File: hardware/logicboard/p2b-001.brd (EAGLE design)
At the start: 91 x 90 mm, 54 parts, among them IC1 74LS06N, IC2 4066N, J1 MKR, J2 GPIO, J3 Vcc, J4 RLY, J5 SPI, J7 DIN5, J8 DIN5, J9 DIN5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

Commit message: Renumbered signal names and silk patterns.
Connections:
- removed net ANLG4: IC2.11, MC1.P$28, RN1.5
- removed net DTCT4: MC1.P$1, SV1.15, SV3.14
- removed net GPIO2: J2.3, MC1.P$5, SV3.10
- removed net LED2: MC1.P$2, R5.2, SV2.17
- new net ANLG0: IC2.1, MC1.P$31, RN1.2
- new net DTCT0: MC1.P$7, SV1.3, SV3.11
- new net GPIO0: J2.2, MC1.P$8, SV3.9
- new net LED0: MC1.P$34, R4.2, SV2.9
- net ANLG1: now also IC2.4, MC1.P$30, RN1.3; no longer IC2.1, MC1.P$31, RN1.2
- net ANLG2: now also IC2.8, MC1.P$29, RN1.4; no longer IC2.4, MC1.P$30, RN1.3
- net ANLG3: now also IC2.11, MC1.P$28, RN1.5; no longer IC2.8, MC1.P$29, RN1.4
- net DTCT1: now also MC1.P$4, SV1.7, SV3.12; no longer MC1.P$7, SV1.3, SV3.11
- net DTCT2: now also MC1.P$3, SV1.11, SV3.13; no longer MC1.P$4, SV1.7, SV3.12
- net DTCT3: now also MC1.P$1, SV1.15, SV3.14; no longer MC1.P$3, SV1.11, SV3.13
- net GPIO1: now also J2.3, MC1.P$5, SV3.10; no longer J2.2, MC1.P$8, SV3.9
- net LED1: now also MC1.P$2, R5.2, SV2.17; no longer MC1.P$34, R4.2, SV2.9
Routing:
- net GPIO2: track 146.6 -> 0.00 mm, vias 2 -> 0
- net LED0: track 0.00 -> 141.5 mm, vias 0 -> 4
- net GPIO0: track 0.00 -> 118.0 mm, vias 0 -> 2
- net LED2: track 115.8 -> 0.00 mm
- net DTCT4: track 99.1 -> 0.00 mm, vias 2 -> 0
- net ANLG4: track 97.6 -> 0.00 mm, vias 4 -> 0
- net DTCT0: track 0.00 -> 77.0 mm, vias 0 -> 4
- net ANLG0: track 0.00 -> 64.4 mm, vias 0 -> 5
- net ANLG1: track 64.4 -> 96.4 mm, vias 5 -> 3
- net GPIO1: track 118.0 -> 146.6 mm
- net DTCT2: track 85.3 -> 112.2 mm, vias 3 -> 4
- net LED1: track 141.5 -> 115.8 mm, vias 4 -> 0
- net DTCT3: track 112.2 -> 99.1 mm, vias 4 -> 2
- net DTCT1: track 77.0 -> 85.3 mm, vias 4 -> 3
- net ANLG2: track 96.4 -> 103.3 mm, vias 3 -> 7
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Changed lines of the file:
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@@
 <grid distance="0.5" unitdist="mm" unit="mm" style="lines" multiple="2" display="yes" altdistance="50" altunitdist="mil" altunit="mil"/>
 <layers>
-<layer number="1" name="Top" color="4" fill="1" visible="yes" active="yes"/>
-<layer number="16" name="Bottom" color="1" fill="1" visible="yes" active="yes"/>
+<layer number="1" name="Top" color="4" fill="1" visible="no" active="yes"/>
+<layer number="16" name="Bottom" color="1" fill="1" visible="no" active="yes"/>
 <layer number="17" name="Pads" color="2" fill="1" visible="yes" active="yes"/>
 <layer number="18" name="Vias" color="2" fill="1" visible="yes" active="yes"/>
@@
 <wire x1="12.954" y1="31.5468" x2="13" y2="31.5" width="0.1524" layer="16"/>
 </signal>
-<signal name="ANLG4" class="3">
+<signal name="ANLG3" class="3">
 <contactref element="MC1" pad="P$28"/>
 <contactref element="IC2" pad="11"/>
@@
 <via x="59.5122" y="46.482" extent="1-16" drill="0.3048"/>
 </signal>
-<signal name="ANLG3" class="3">
+<signal name="ANLG2" class="3">
 <contactref element="MC1" pad="P$29"/>
 <contactref element="IC2" pad="8"/>
@@
 <via x="35.5092" y="77.1906" extent="1-16" drill="0.3048"/>
 </signal>
-<signal name="ANLG2" class="3">
+<signal name="ANLG1" class="3">
 <contactref element="MC1" pad="P$30"/>
 <contactref element="IC2" pad="4"/>
@@
 <via x="58.5216" y="82.9818" extent="1-16" drill="0.3048"/>
 </signal>
-<signal name="ANLG1" class="3">
+<signal name="ANLG0" class="3">
 <contactref element="MC1" pad="P$31"/>
 <contactref element="IC2" pad="1"/>
@@
 <wire x1="44.577" y1="65.4558" x2="44.62" y2="65.5" width="0.1524" layer="16"/>
 </signal>
-<signal name="DTCT1">
+<signal name="DTCT0">
 <contactref element="MC1" pad="P$7"/>
 <contactref element="SV1" pad="3"/>
@@
 <via x="50.0634" y="61.2648" extent="1-16" drill="0.3048"/>
 </signal>
-<signal name="DTCT2">
+<signal name="DTCT1">
 <contactref element="MC1" pad="P$4"/>
 <contactref element="SV1" pad="7"/>
@@
 <via x="49.2252" y="76.7334" extent="1-16" drill="0.3048"/>
 </signal>
-<signal name="DTCT3">
+<signal name="DTCT2">
 <contactref element="MC1" pad="P$3"/>
 <contactref element="SV1" pad="11"/>
@@
 <via x="39.0144" y="62.484" extent="1-16" drill="0.3048"/>
 </signal>
-<signal name="DTCT4">
+<signal name="DTCT3">
 <contactref element="MC1" pad="P$1"/>
 <contactref element="SV1" pad="15"/>
@@
 <via x="69.342" y="27.8892" extent="1-16" drill="0.3048"/>
 </signal>
-<signal name="LED1">
+<signal name="LED0">
 <contactref element="MC1" pad="P$34"/>
 <contactref element="R4" pad="2"/>
@@
 <contactref element="MC1" pad="P$33"/>
 </signal>
-<signal name="LED2">
+<signal name="LED1">
 <contactref element="MC1" pad="P$2"/>
 <contactref element="R5" pad="2"/>
@@
 <via x="57.912" y="70.4088" extent="1-16" drill="0.3048"/>
 </signal>
-<signal name="GPIO2">
+<signal name="GPIO1">
 <contactref element="MC1" pad="P$5"/>
 <contactref element="J2" pad="3"/>
@@
 <via x="16.9926" y="21.6408" extent="1-16" drill="0.3048"/>
 </signal>
-<signal name="GPIO1">
+<signal name="GPIO0">
 <contactref element="MC1" pad="P$8"/>
 <contactref element="J2" pad="2"/>

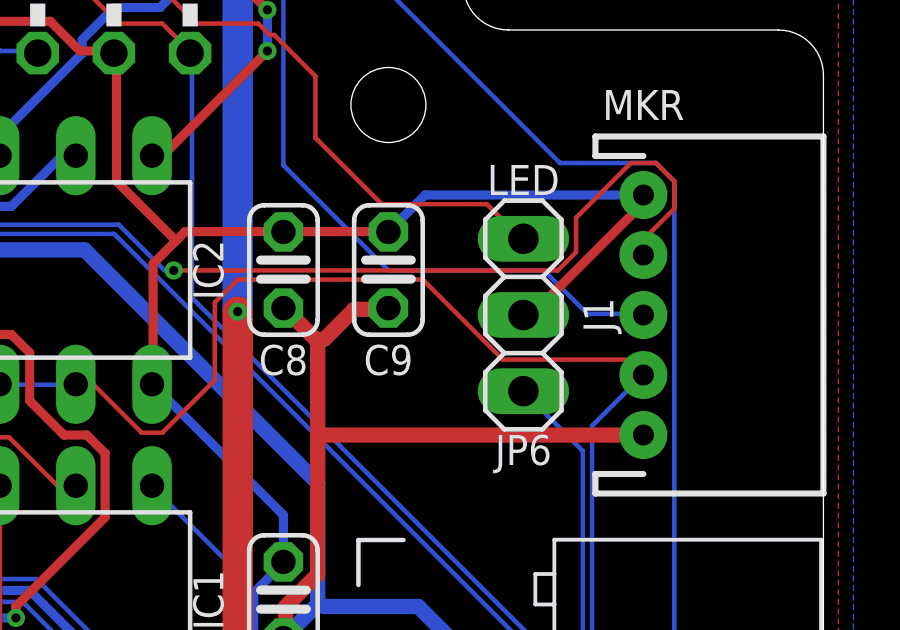
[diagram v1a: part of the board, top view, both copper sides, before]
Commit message: Added silk of LED0/1.
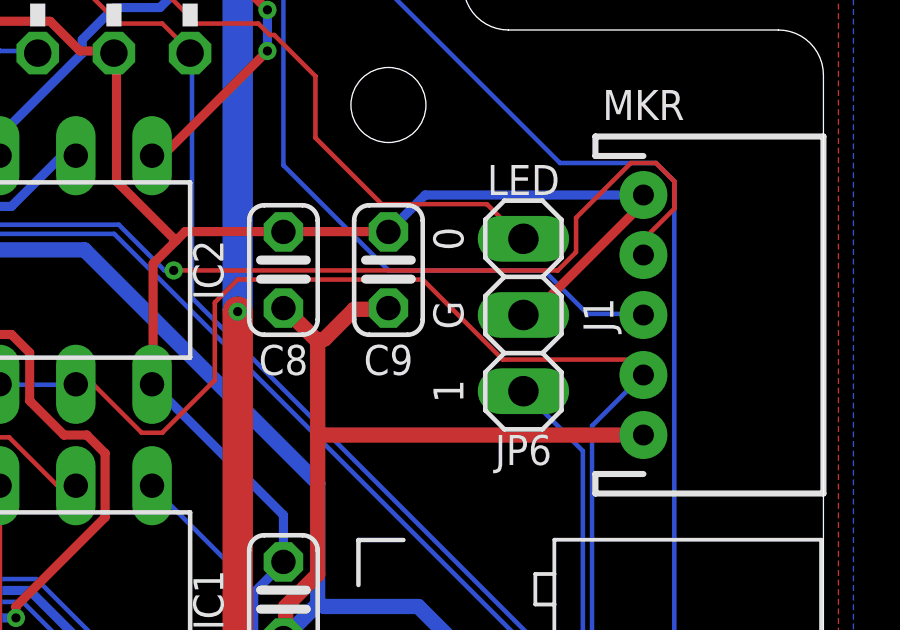
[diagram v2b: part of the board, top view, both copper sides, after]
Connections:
- removed net LED2A: JP6.1, R5.1
- new net LED0A: JP6.3, R4.1
- net LED1A: now also JP6.1, R5.1; no longer JP6.3, R4.1
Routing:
- net LED0A: track 0.00 -> 109.4 mm, vias 0 -> 2
- net LED2A: track 78.2 -> 0.00 mm, vias 3 -> 0
- net LED1A: track 109.4 -> 78.2 mm, vias 2 -> 3
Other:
- board text added: "0"
- board text added: "1"
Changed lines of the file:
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@@
 <wire x1="63.04" y1="33.5" x2="63.04" y2="32.5" width="0.15" layer="21"/>
 <text x="63.54" y="34.5" size="1" layer="25" align="center">LED00</text>
+<text x="79" y="71.54" size="1" layer="25" rot="R90" align="bottom-center">0</text>
+<text x="79" y="66.46" size="1" layer="25" rot="R90" align="bottom-center">1</text>
+<text x="79" y="69" size="1" layer="25" rot="R90" align="bottom-center">G</text>
 </plain>
 <attributes>
@@
 <wire x1="70.3326" y1="43.2054" x2="70.39" y2="43.19" width="0.1524" layer="16"/>
 </signal>
-<signal name="LED1A">
+<signal name="LED0A">
 <contactref element="R4" pad="1"/>
 <contactref element="JP6" pad="3"/>
@@
 <via x="66.5226" y="82.4484" extent="1-16" drill="0.3048"/>
 </signal>
-<signal name="LED2A">
+<signal name="LED1A">
 <contactref element="R5" pad="1"/>
 <contactref element="JP6" pad="1"/>

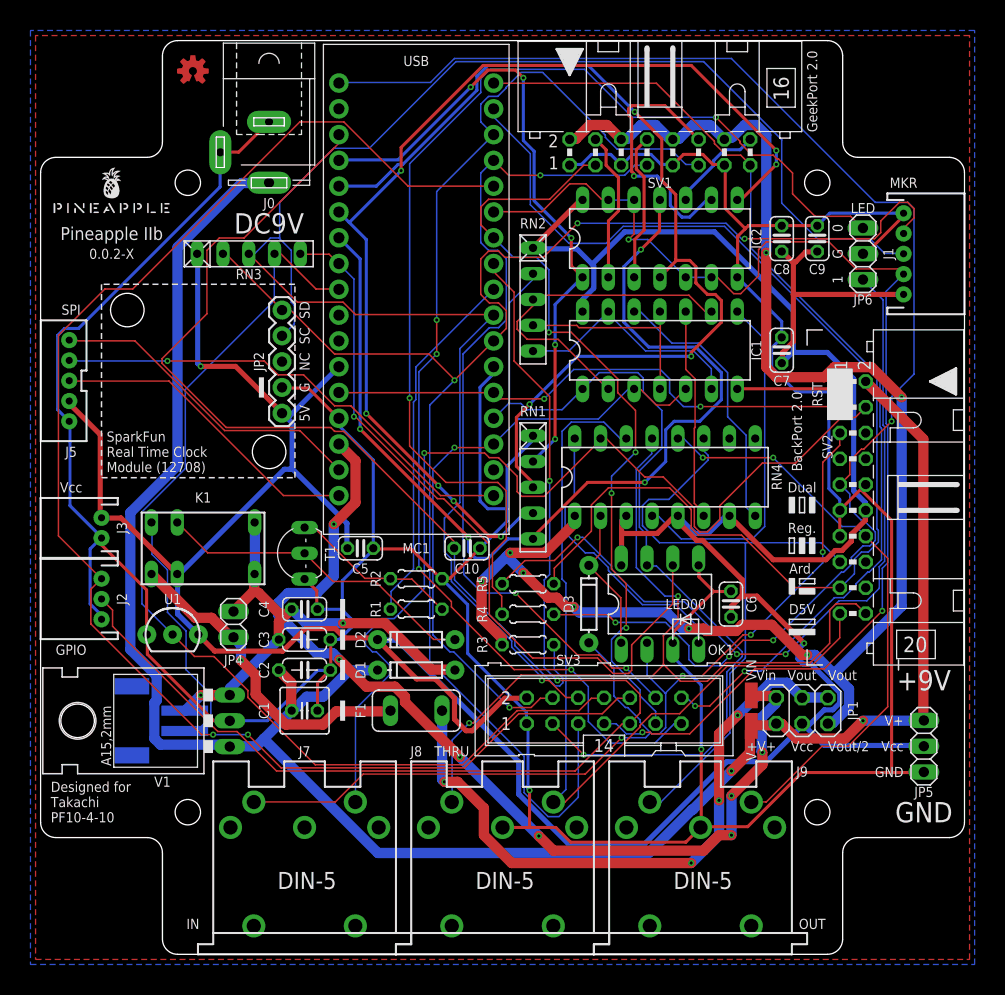
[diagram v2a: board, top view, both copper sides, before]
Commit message: Added J6 (LED connector).
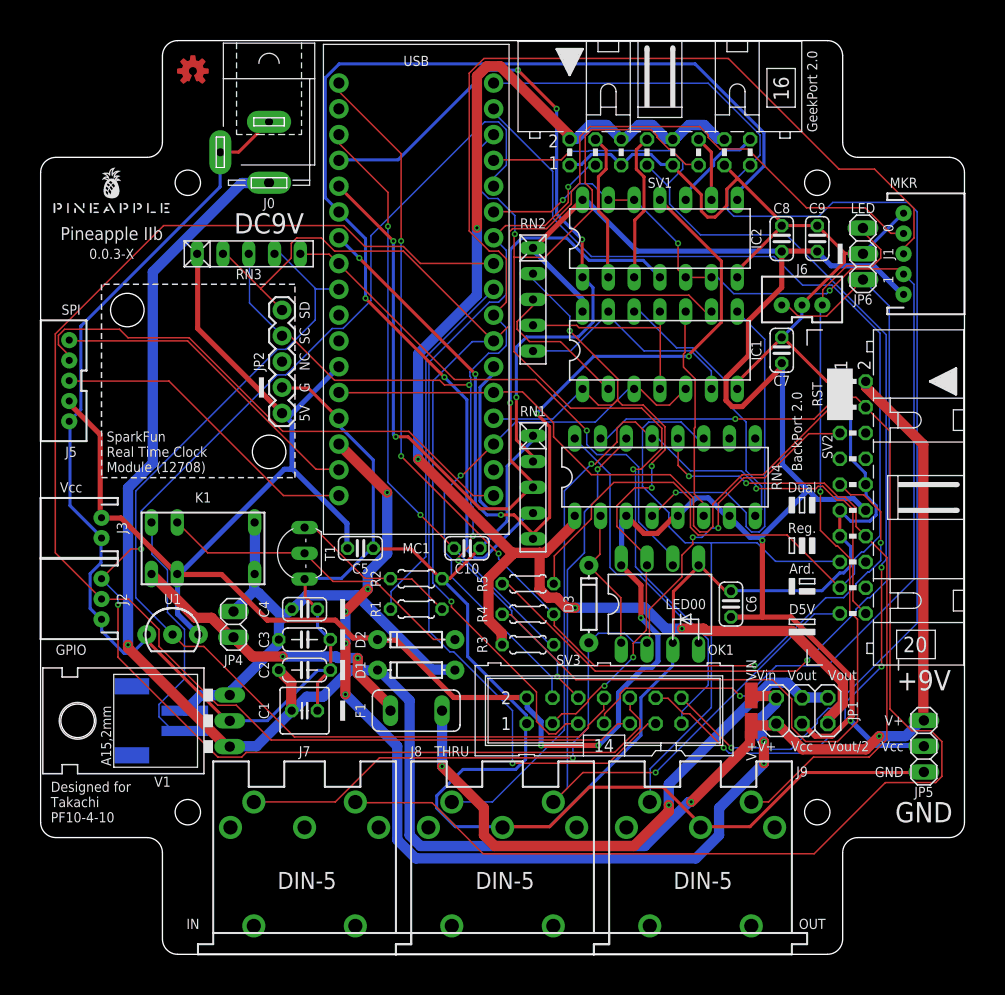
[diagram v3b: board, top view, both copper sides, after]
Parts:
- added J6: (no value), SparkFun-Connectors:JST-3-PTH-VERT
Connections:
- net GND: now also J6.2
- net LED0A: now also J6.3
- net LED1A: now also J6.1
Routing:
- net VCC: track 365.7 -> 325.5 mm, vias 2 -> 5
- net MISND: track 99.5 -> 131.9 mm
- net AREF: track 90.6 -> 59.2 mm, vias 0 -> 2
- net LED0: track 141.5 -> 110.3 mm, vias 4 -> 5
- net DTCT1: track 85.3 -> 115.8 mm, vias 3 -> 4
- net DTCT3: track 99.1 -> 128.2 mm, vias 2 -> 1
- net MNTR: track 73.9 -> 53.9 mm
- net ANLG3R: track 26.2 -> 6.48 mm, vias 1 -> 0
- net GPIO0: track 118.0 -> 136.6 mm, vias 2 -> 0
- net RX: track 92.4 -> 74.2 mm, vias 1 -> 5
- net MIRTN: track 98.6 -> 84.2 mm, vias 4 -> 3
- net DTCT0: track 77.0 -> 89.2 mm, vias 4 -> 2
- net ANLG2: track 103.3 -> 115.2 mm, vias 7 -> 2
- net LED0A: track 109.4 -> 97.6 mm, vias 2 -> 1
- net SCL: track 169.6 -> 157.9 mm, vias 1 -> 4
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- removed copper zone on layer 1, net GND
- removed copper zone on layer 16, net GND
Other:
- board text added: "0.0.3-X"
- board text removed: "0.0.2-X"

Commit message: Re-arranged GeekPort 2.0.
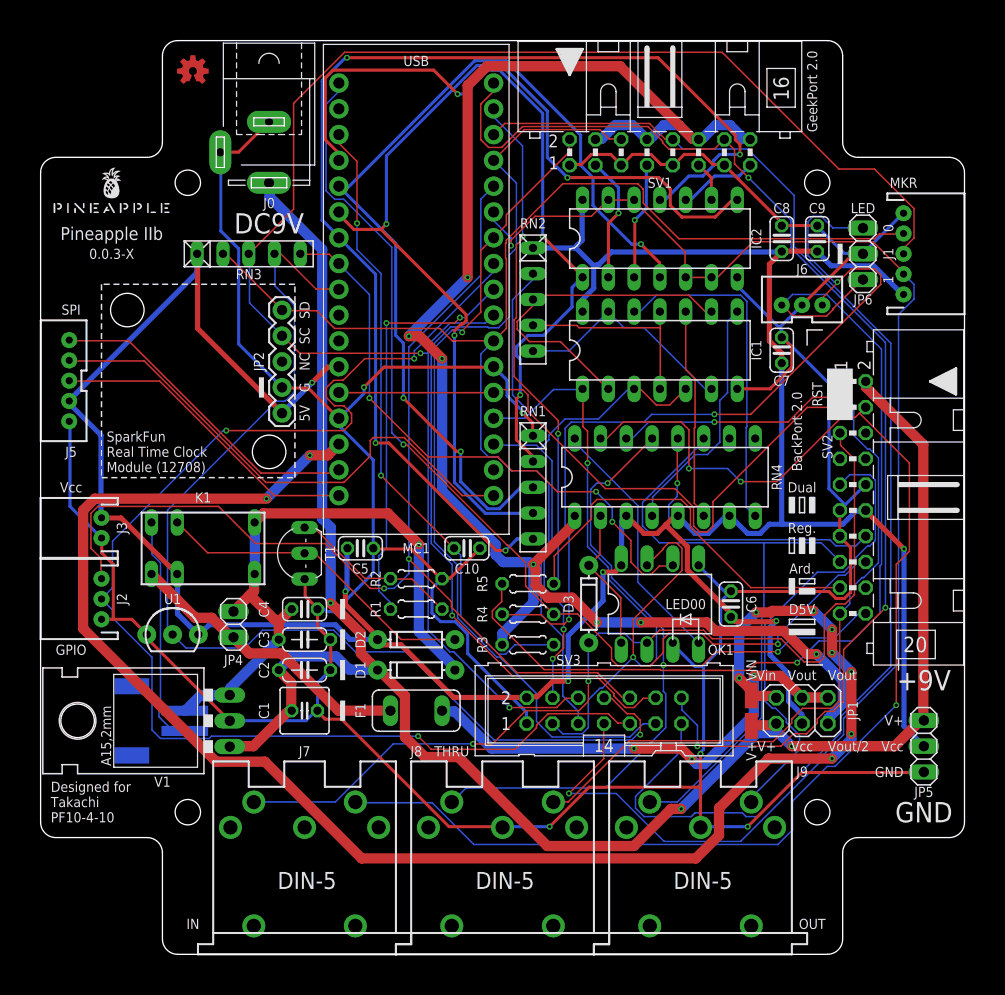
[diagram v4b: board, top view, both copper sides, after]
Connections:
- removed net ANLG4R: IC2.10, SV1.16
- new net ANLG0R: IC2.2, SV1.3
- net ANLG1R: now also IC2.3, SV1.7; no longer IC2.2, SV1.4
- net ANLG2R: now also IC2.9, SV1.11; no longer IC2.3, SV1.8
- net ANLG3R: now also IC2.10, SV1.15; no longer IC2.9, SV1.12
- net DTCT0: now also SV1.2; no longer SV1.3
- net DTCT1: now also SV1.6; no longer SV1.7
- net DTCT2: now also SV1.10; no longer SV1.11
- net DTCT3: now also SV1.14; no longer SV1.15
- net VCC/2: now also SV1.12, SV1.16, SV1.4, SV1.8; no longer SV1.10, SV1.14, SV1.2, SV1.6
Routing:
- net VIN: track 96.8 -> 162.8 mm, vias 7 -> 10
- net LED1: track 117.6 -> 89.0 mm, vias 0 -> 2
- net GPIO1: track 139.3 -> 111.8 mm
- net D7GATE: track 117.1 -> 143.0 mm, vias 4 -> 2
- net ANLG3: track 89.3 -> 115.1 mm, vias 5 -> 4
- net GND: track 423.9 -> 398.8 mm, vias 0 -> 5
- net DTCT1: track 115.8 -> 91.5 mm, vias 4 -> 1
- net SDA: track 151.0 -> 130.2 mm, vias 1 -> 0
- net VCC: track 325.5 -> 305.2 mm, vias 5 -> 6
- net DTCT2: track 106.6 -> 126.4 mm, vias 2 -> 0
- net V+: track 202.0 -> 184.0 mm
- net ANLG2: track 115.2 -> 99.2 mm, vias 2 -> 3
- net MTSND: track 74.7 -> 88.8 mm
- net RX: track 74.2 -> 88.3 mm, vias 5 -> 2
- net VCC/2: track 145.3 -> 158.8 mm, vias 4 -> 7
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
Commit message: Fixed silk.
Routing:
- added copper zone on layer 1, net GND
- added copper zone on layer 16, net GND
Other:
- board text added: "2.5.0-RC"
- board text added: "BackPort II"
- board text added: "GeekPort II"
- board text removed: "0.0.3-X"
- board text removed: "BackPort 2.0"
- board text removed: "GeekPort 2.0"
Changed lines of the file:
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@@
 <setting verticaltext="up"/>
 </settings>
-<grid distance="0.5" unitdist="mm" unit="mm" style="lines" multiple="2" display="yes" altdistance="50" altunitdist="mil" altunit="mil"/>
+<grid distance="1" unitdist="mm" unit="mm" style="lines" multiple="1" display="yes" altdistance="50" altunitdist="mil" altunit="mil"/>
 <layers>
 <layer number="1" name="Top" color="4" fill="1" visible="yes" active="yes"/>
@@
 <wire x1="25.05" y1="66" x2="6" y2="66" width="0.15" layer="21" style="dashdot"/>
 <wire x1="6" y1="66" x2="6" y2="46.95" width="0.15" layer="21" style="dashdot"/>
-<text x="7" y="69" size="1" layer="25" align="center">0.0.3-X</text>
+<text x="7" y="69" size="1" layer="25" align="center">2.5.0-RC</text>
 <text x="26" y="63.46" size="1" layer="25" rot="R90" align="center">SD</text>
 <text x="26" y="60.92" size="1" layer="25" rot="R90" align="center">SC</text>
@@
 <vertex x="12" y="11.5"/>
 </polygon>
-<text x="76" y="85" size="1" layer="25" rot="R90" align="center">GeekPort 2.0</text>
-<text x="74.5" y="51.5" size="1" layer="25" rot="R90" align="center">BackPort 2.0</text>
+<text x="76" y="85" size="1" layer="25" rot="R90" align="center">GeekPort II</text>
+<text x="74.5" y="51.5" size="1" layer="25" rot="R90" align="center">BackPort II</text>
 <wire x1="64.81" y1="31" x2="64.81" y2="33" width="0.15" layer="21"/>
 <wire x1="64.81" y1="33" x2="63.04" y2="33" width="0.15" layer="21"/>
@@
 <via x="31.8516" y="55.8546" extent="1-16" drill="0.3048"/>
 <via x="50.1396" y="12.573" extent="1-16" drill="0.3048"/>
+<polygon width="0.2" layer="1">
+<vertex x="-1" y="-1"/>
+<vertex x="92" y="-1"/>
+<vertex x="92" y="91"/>
+<vertex x="-1" y="91"/>
+</polygon>
+<polygon width="0.2" layer="16">
+<vertex x="-2" y="-2"/>
+<vertex x="93" y="-2"/>
+<vertex x="93" y="92"/>
+<vertex x="-2" y="92"/>
+</polygon>
 </signal>
 <signal name="VCC" class="2">
